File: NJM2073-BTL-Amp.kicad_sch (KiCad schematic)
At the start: 86 parts, among them J1 Screw_Terminal_01x02, J2 Screw_Terminal_01x02, J3 Barrel_Jack_Switch, J4 Conn_Coaxial_x2, J5 AudioJack3_SwitchTR, U1 NJM2073, U2 NJM2073, U3 NJM4558, U4 NJM4558, U5 LM317_TO-220

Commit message: 除外設定を解除
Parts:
- U1, U2: now in the parts list
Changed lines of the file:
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@@
 		(unit 1)
 		(exclude_from_sim no)
-		(in_bom no)
-		(on_board no)
+		(in_bom yes)
+		(on_board yes)
 		(dnp no)
 		(fields_autoplaced yes)
@@
 		(unit 1)
 		(exclude_from_sim no)
-		(in_bom no)
-		(on_board no)
+		(in_bom yes)
+		(on_board yes)
 		(dnp no)
 		(fields_autoplaced yes)
@@
 		(unit 2)
 		(exclude_from_sim no)
-		(in_bom no)
-		(on_board no)
+		(in_bom yes)
+		(on_board yes)
 		(dnp no)
 		(fields_autoplaced yes)
@@
 		(unit 2)
 		(exclude_from_sim no)
-		(in_bom no)
-		(on_board no)
+		(in_bom yes)
+		(on_board yes)
 		(dnp no)
 		(fields_autoplaced yes)

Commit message: フットプリント変更
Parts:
- U3, U4: footprint Package_DIP:DIP-8_W7.62mm -> Package_DIP:DIP-8_W7.62mm_Socket
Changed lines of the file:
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@@
 			)
 		)
-		(property "Footprint" "Package_DIP:DIP-8_W7.62mm"
+		(property "Footprint" "Package_DIP:DIP-8_W7.62mm_Socket"
 			(at 152.4 177.8 0)
 			(effects
@@
 			)
 		)
-		(property "Footprint" "Package_DIP:DIP-8_W7.62mm"
+		(property "Footprint" "Package_DIP:DIP-8_W7.62mm_Socket"
 			(at 215.9 165.1 0)
 			(effects
@@
 			)
 		)
-		(property "Footprint" "Package_DIP:DIP-8_W7.62mm"
+		(property "Footprint" "Package_DIP:DIP-8_W7.62mm_Socket"
 			(at 152.4 88.9 0)
 			(effects
@@
 			)
 		)
-		(property "Footprint" "Package_DIP:DIP-8_W7.62mm"
+		(property "Footprint" "Package_DIP:DIP-8_W7.62mm_Socket"
 			(at 166.37 46.99 0)
 			(effects
@@
 			)
 		)
-		(property "Footprint" "Package_DIP:DIP-8_W7.62mm"
+		(property "Footprint" "Package_DIP:DIP-8_W7.62mm_Socket"
 			(at 166.37 135.89 0)
 			(effects
@@
 			)
 		)
-		(property "Footprint" "Package_DIP:DIP-8_W7.62mm"
+		(property "Footprint" "Package_DIP:DIP-8_W7.62mm_Socket"
 			(at 215.9 76.2 0)
 			(effects

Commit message: フットプリント変更
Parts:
- L1, L2: footprint Capacitor_THT:CP_Radial_D10.0mm_P5.00mm -> Inductor_THT:L_Radial_D10.0mm_P5.00mm_Fastron_07M
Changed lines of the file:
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@@
 			)
 		)
-		(property "Footprint" "Capacitor_THT:CP_Radial_D10.0mm_P5.00mm"
+		(property "Footprint" "Inductor_THT:L_Radial_D10.0mm_P5.00mm_Fastron_07M"
 			(at 57.15 25.4 0)
 			(effects
@@
 			)
 		)
-		(property "Footprint" "Capacitor_THT:CP_Radial_D10.0mm_P5.00mm"
+		(property "Footprint" "Inductor_THT:L_Radial_D10.0mm_P5.00mm_Fastron_07M"
 			(at 69.85 25.4 0)
 			(effects

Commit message: 部品の向き修正
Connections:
- net GND: now also C12.1; no longer C12.2
- net at C16.2, U1.5 (BIN-): now also C12.2; no longer C12.1
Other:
- moved on the sheet: C12
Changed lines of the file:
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@@
 	(symbol
 		(lib_id "Device:C")
-		(at 304.8 95.25 0)
+		(at 304.8 95.25 180)
 		(unit 1)
 		(exclude_from_sim no)
@@
 					(size 1.27 1.27)
 				)
-				(justify left)
+				(justify right)
 			)
 		)
@@
 					(size 1.27 1.27)
 				)
-				(justify left)
+				(justify right)
 			)
 		)
 		(property "Footprint" "Capacitor_THT:C_Disc_D5.0mm_W2.5mm_P5.00mm"
-			(at 305.7652 99.06 0)
+			(at 303.8348 91.44 0)
 			(effects
 				(font

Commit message: BTL アンプ部構成・アンプ電源配置配線
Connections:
- net GND: now also C14.1; no longer C14.2
- net at C18.2, U2.5 (BIN-): now also C14.2; no longer C14.1
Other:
- moved on the sheet: C14
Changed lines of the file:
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@@
 	(symbol
 		(lib_id "Device:C")
-		(at 304.8 184.15 0)
+		(at 304.8 184.15 180)
 		(unit 1)
 		(exclude_from_sim no)
@@
 					(size 1.27 1.27)
 				)
-				(justify left)
+				(justify right)
 			)
 		)
@@
 					(size 1.27 1.27)
 				)
-				(justify left)
+				(justify right)
 			)
 		)
 		(property "Footprint" "Capacitor_THT:C_Disc_D5.0mm_W2.5mm_P5.00mm"
-			(at 305.7652 187.96 0)
+			(at 303.8348 180.34 0)
 			(effects
 				(font

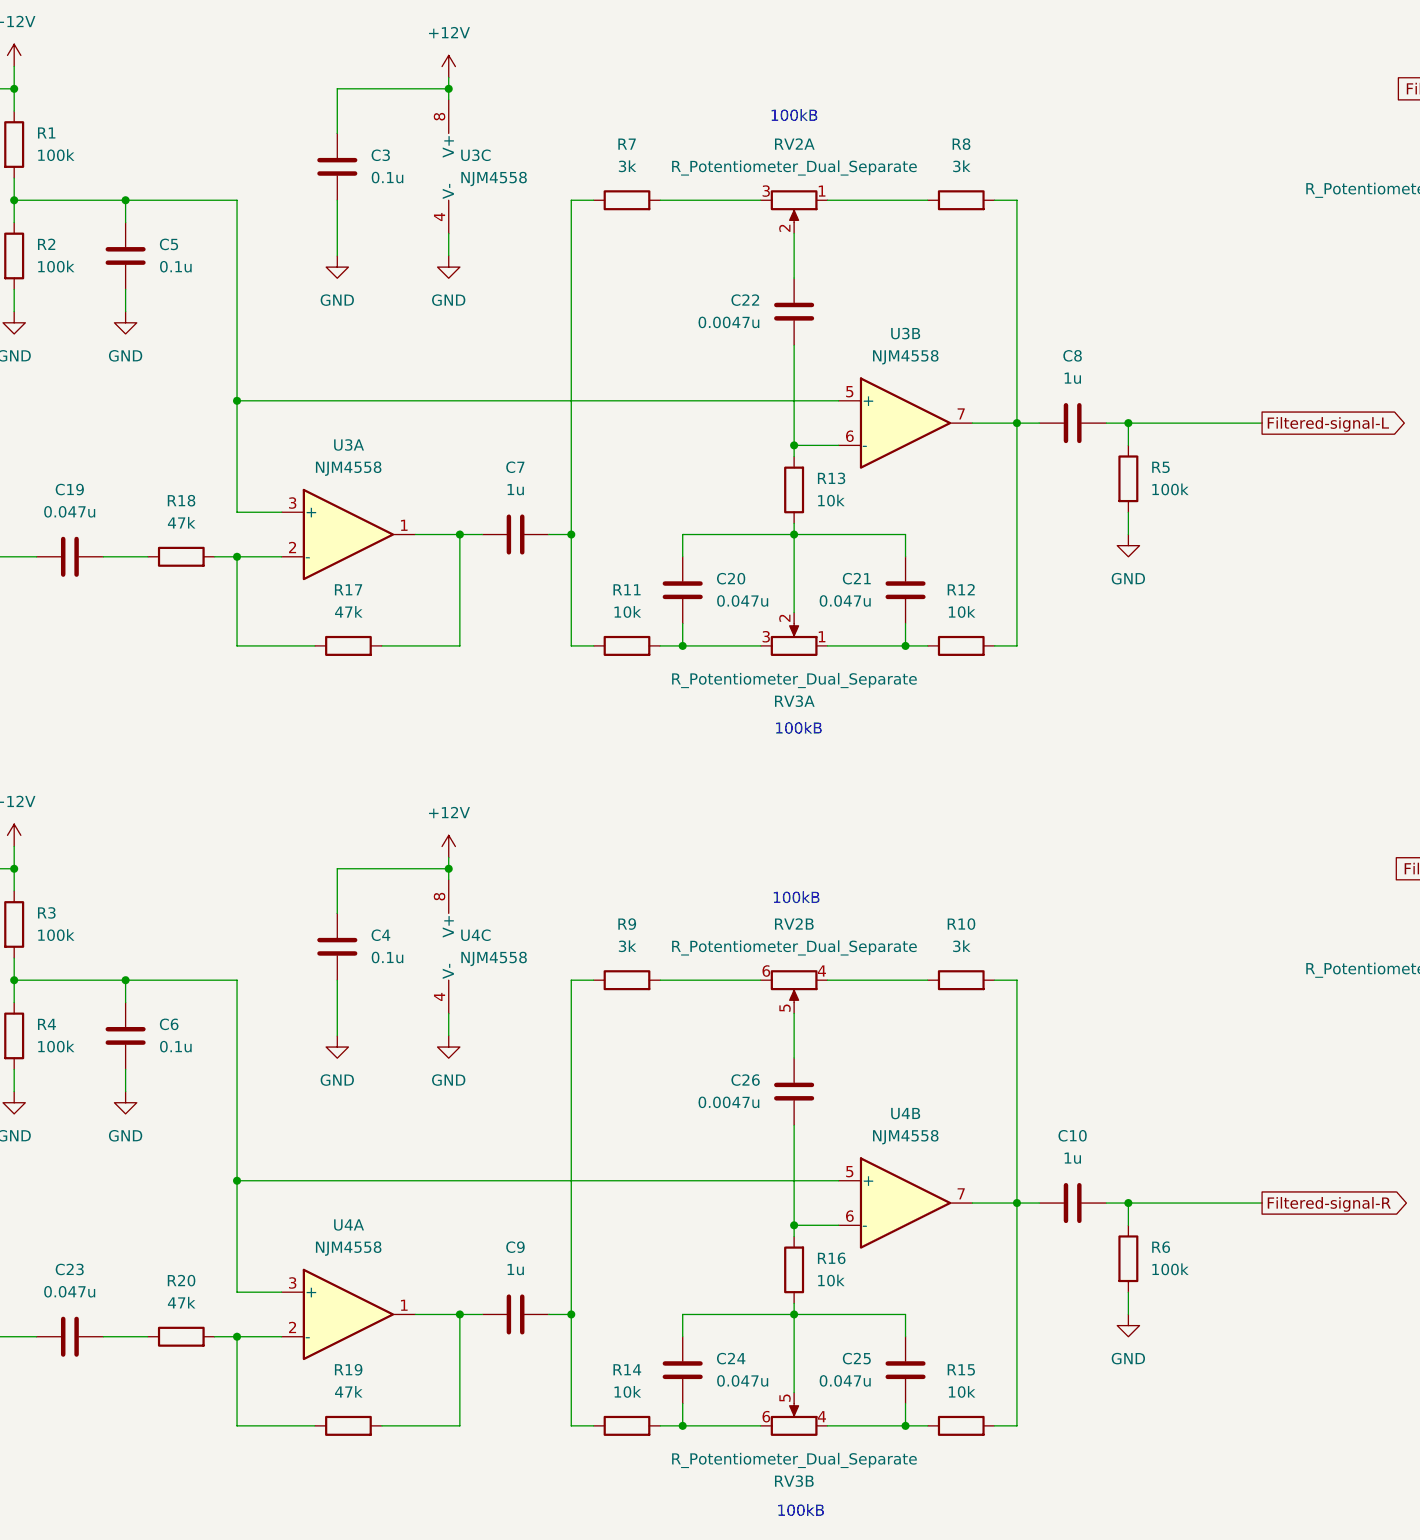
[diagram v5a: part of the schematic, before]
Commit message: 部品結線変更
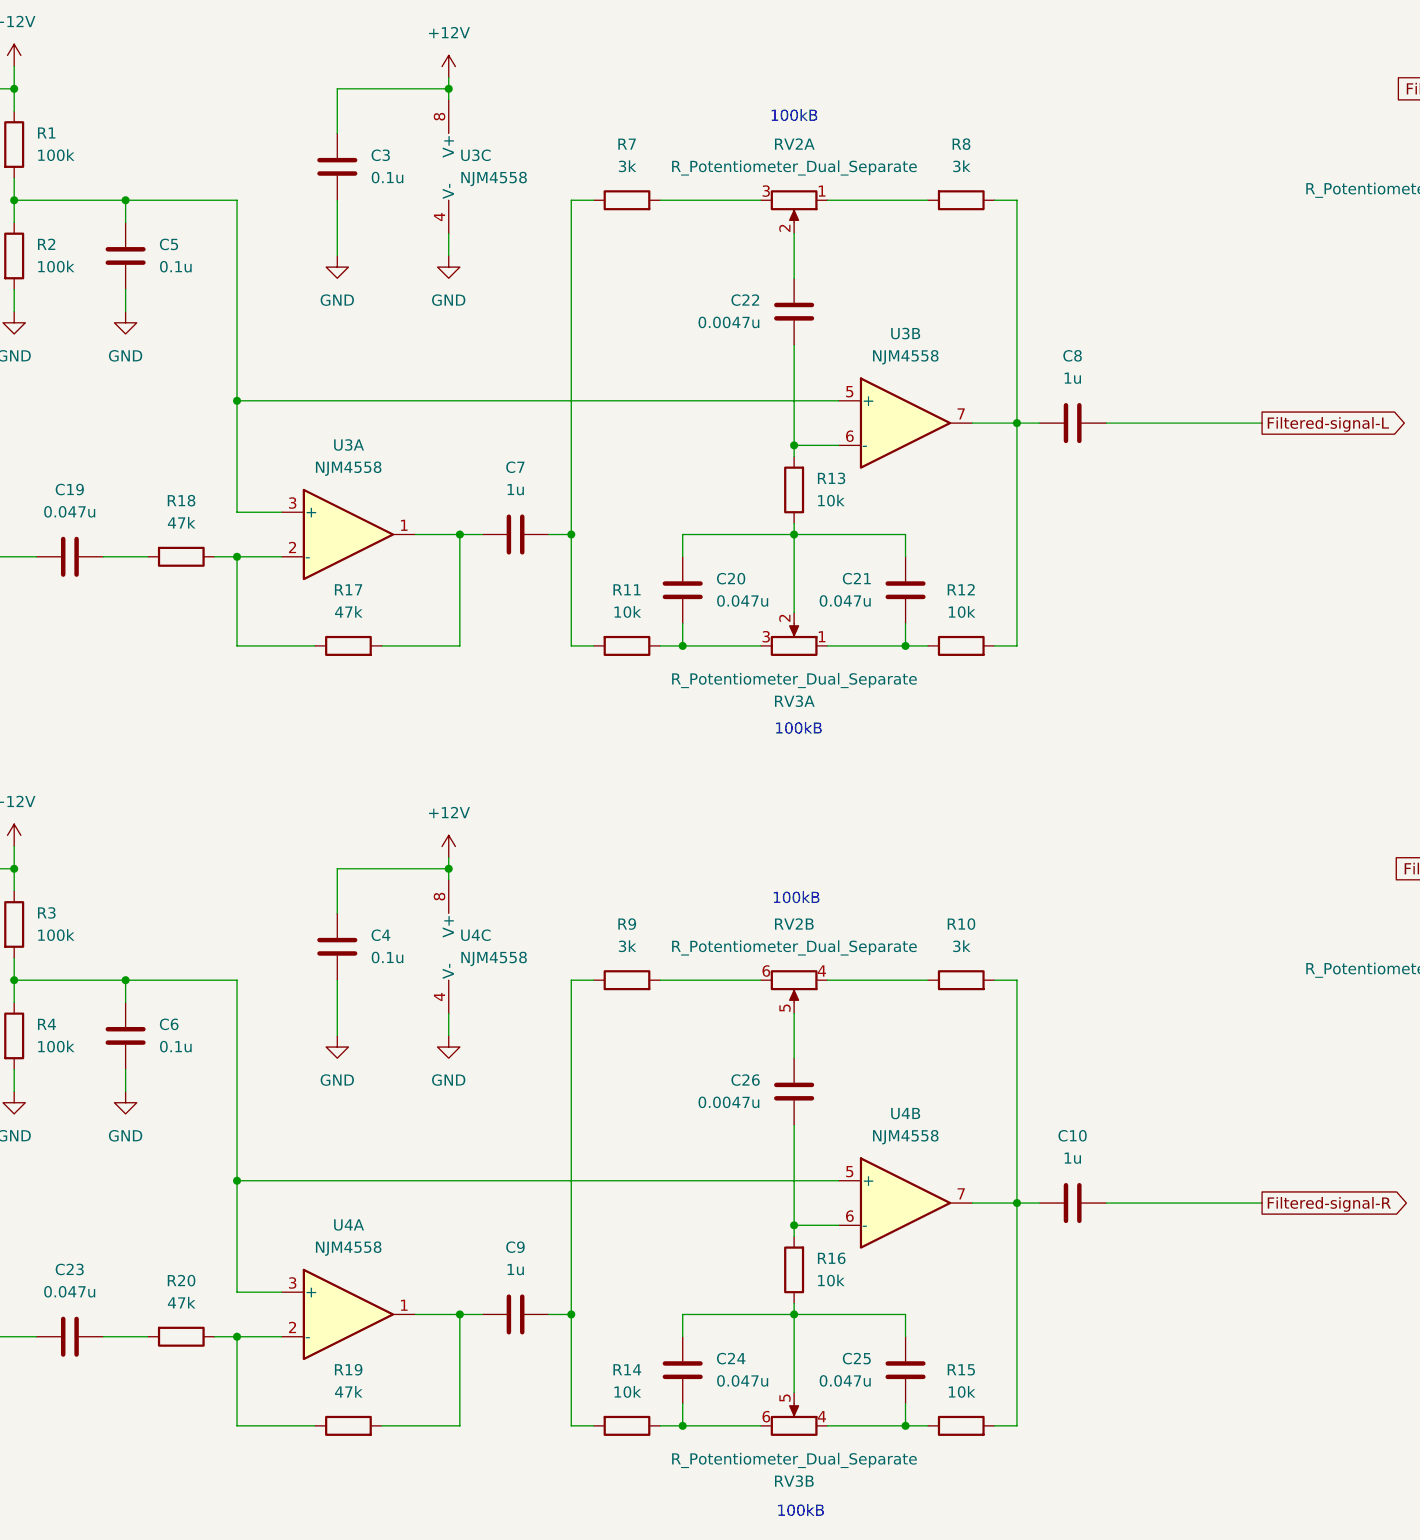
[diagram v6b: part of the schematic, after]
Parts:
- removed R5, R6: 100k, Resistor_THT:R_Axial_DIN0207_L6.3mm_D2.5mm_P10.16mm_Horizontal, symbol Device:R
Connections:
- net +12V: now also C3.2, C4.2; no longer C3.1, C4.1
- net GND: now also C3.1, C4.1; no longer C3.2, C4.2
- net at RV2.1: now also R8.2; no longer R8.1
- net at C7.2, R7.1: now also R11.2; no longer R11.1
- net at R19.1, U4.2 (-): now also R20.1; no longer R20.2
- net at C8.1, R12.2, U3.7: now also R8.1; no longer R8.2
- net at C19.2: now also R18.2; no longer R18.1
- net at C24.1, RV3.6: now also R14.1; no longer R14.2
- net at C9.2, R9.1: now also R14.2; no longer R14.1
- net at R17.1, U3.2 (-): now also R18.1; no longer R18.2
- net at C20.1, RV3.3: now also R11.1; no longer R11.2
- net at C23.2: now also R20.2; no longer R20.1
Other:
- moved on the sheet: C3, C4, R11, R14, R18, R20, R8

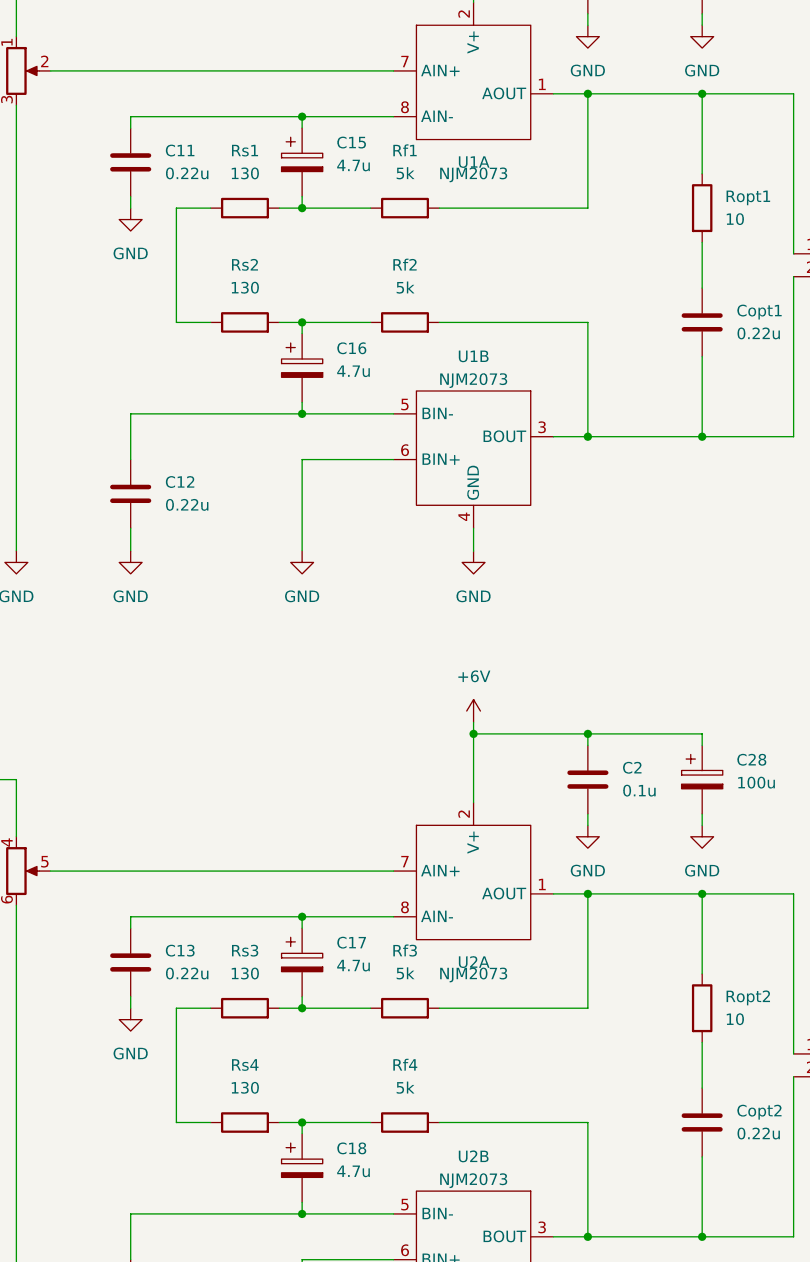
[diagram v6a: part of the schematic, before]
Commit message: 抵抗値修正
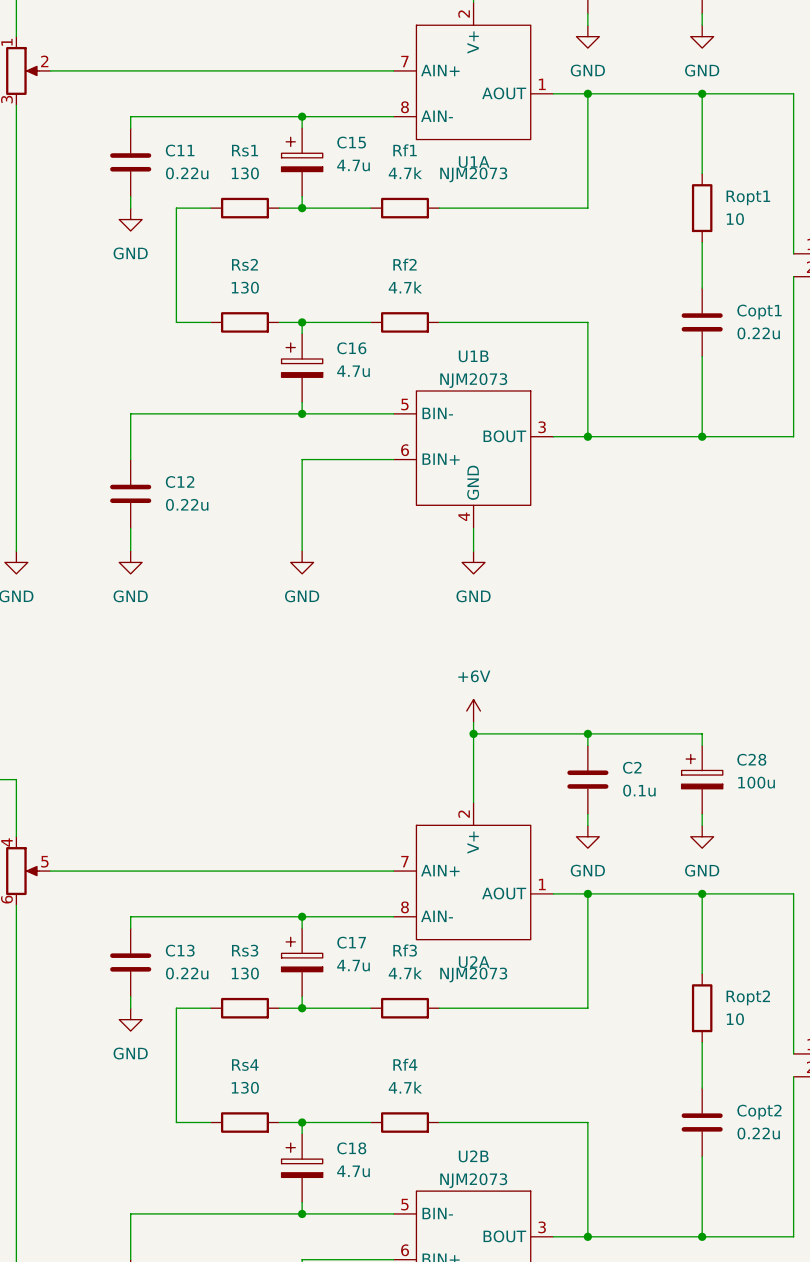
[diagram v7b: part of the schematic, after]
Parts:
- Rf1, Rf2, Rf3, Rf4: value 5k -> 4.7k
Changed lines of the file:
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@@
 			)
 		)
-		(property "Value" "5k"
+		(property "Value" "4.7k"
 			(at 335.28 59.69 90)
 			(effects
@@
 			)
 		)
-		(property "Value" "5k"
+		(property "Value" "4.7k"
 			(at 335.28 72.39 90)
 			(effects
@@
 			)
 		)
-		(property "Value" "5k"
+		(property "Value" "4.7k"
 			(at 335.28 148.59 90)
 			(effects
@@
 			)
 		)
-		(property "Value" "5k"
+		(property "Value" "4.7k"
 			(at 335.28 161.29 90)
 			(effects
